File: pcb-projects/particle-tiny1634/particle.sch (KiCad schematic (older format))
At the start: 31 parts, among them CON1 AVR-ISP-6, IC1 ATTINY1634-SU, P1 TXN, P2 RXN, P3 TXS, P4 RXS, P5 TRX-CH, P6 TEST1-3

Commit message: added all 3d models, pcb cosmetics
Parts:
- FB1, FB2: footprint SMD_Packages:SMD-2010_Pol -> SMD_Packages:SMD-1206_Pol
- P1, P2: footprint SMT_PIN_HEADER:CONN-8_1-4 -> SMT_PIN_HEADER:CONN-6_1-3; symbol CONN_01X04 -> CONN_01X03
- P3, P4: footprint SMT_PIN_HEADER:CONN-8_5-8 -> SMT_PIN_HEADER:CONN-6_4-6; symbol CONN_02X04 -> CONN_02X03
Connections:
- net GND: now also P4.6 (P6); no longer P1.2 (P2), P4.7 (P7), P4.8 (P8)
- net RX-SOUTH: now also P4.4 (P4); no longer P4.5 (P5)
- net TX-NORTH: now also P1.3 (P3); no longer P1.4 (P4)
- net TX-SOUTH: now also P3.6 (P6); no longer P3.8 (P8)
- net VCC: now also P3.4 (P4); no longer P2.4 (P4), P3.5 (P5), P3.6 (P6)
- no-connect marks 12 -> 10
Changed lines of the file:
@@
 L VCC #PWR013
 U 1 1 568B8C3F
-P 5800 5100
-F 0 "#PWR013" H 5800 4950 50  0001 C CNN
-F 1 "VCC" H 5800 5250 50  0000 C CNN
-F 2 "" H 5800 5100 50  0000 C CNN
-F 3 "" H 5800 5100 50  0000 C CNN
-	1    5800 5100
-	1    0    0    -1
-$EndComp
-Text Label 4650 4550 0    60   ~ 0
+P 5500 5450
+F 0 "#PWR013" H 5500 5300 50  0001 C CNN
+F 1 "VCC" H 5500 5600 50  0000 C CNN
+F 2 "" H 5500 5450 50  0000 C CNN
+F 3 "" H 5500 5450 50  0000 C CNN
+	1    5500 5450
+	1    0    0    -1
+$EndComp
+Text Label 5850 4600 2    60   ~ 0
 RX-SOUTH
 $Comp
-L CONN_01X04 P2
+L CONN_01X03 P2
 U 1 1 568B98FD
-P 5650 2100
-F 0 "P2" H 5650 2350 50  0000 C CNN
-F 1 "RXN" V 5750 2100 50  0000 C CNN
-F 2 "SMT_PIN_HEADER:CONN-8_1-4" H 5650 2100 50  0001 C CNN
-F 3 "" H 5650 2100 50  0000 C CNN
-	1    5650 2100
+P 5650 2050
+F 0 "P2" H 5650 2300 50  0000 C CNN
+F 1 "RXN" V 5750 2050 50  0000 C CNN
+F 2 "SMT_PIN_HEADER:CONN-6_1-3" H 5650 2050 50  0001 C CNN
+F 3 "" H 5650 2050 50  0000 C CNN
+	1    5650 2050
 	1    0    0    -1
 $EndComp
@@
 L VCC #PWR014
 U 1 1 568B9905
-P 5200 2250
-F 0 "#PWR014" H 5200 2100 50  0001 C CNN
-F 1 "VCC" H 5200 2400 50  0000 C CNN
-F 2 "" H 5200 2250 50  0000 C CNN
-F 3 "" H 5200 2250 50  0000 C CNN
-	1    5200 2250
+P 5200 2150
+F 0 "#PWR014" H 5200 2000 50  0001 C CNN
+F 1 "VCC" H 5200 2300 50  0000 C CNN
+F 2 "" H 5200 2150 50  0000 C CNN
+F 3 "" H 5200 2150 50  0000 C CNN
+	1    5200 2150
 	1    0    0    -1
 $EndComp
 NoConn ~ 5450 2050
 $Comp
-L CONN_01X04 P1
+L CONN_01X03 P1
 U 1 1 568B990C
-P 5650 2700
-F 0 "P1" H 5650 2950 50  0000 C CNN
-F 1 "TXN" V 5750 2700 50  0000 C CNN
-F 2 "SMT_PIN_HEADER:CONN-8_1-4" H 5650 2700 50  0001 C CNN
-F 3 "" H 5650 2700 50  0000 C CNN
-	1    5650 2700
+P 5650 2750
+F 0 "P1" H 5650 3000 50  0000 C CNN
+F 1 "TXN" V 5750 2750 50  0000 C CNN
+F 2 "SMT_PIN_HEADER:CONN-6_1-3" H 5650 2750 50  0001 C CNN
+F 3 "" H 5650 2750 50  0000 C CNN
+	1    5650 2750
 	1    0    0    -1
 $EndComp
@@
 L GND #PWR016
 U 1 1 568BA31C
-P 5200 4800
-F 0 "#PWR016" H 5200 4550 50  0001 C CNN
-F 1 "GND" H 5200 4650 50  0000 C CNN
-F 2 "" H 5200 4800 50  0000 C CNN
-F 3 "" H 5200 4800 50  0000 C CNN
-	1    5200 4800
-	1    0    0    -1
-$EndComp
-Text Label 4650 5700 0    60   ~ 0
+P 5500 4700
+F 0 "#PWR016" H 5500 4450 50  0001 C CNN
+F 1 "GND" H 5500 4550 50  0000 C CNN
+F 2 "" H 5500 4700 50  0000 C CNN
+F 3 "" H 5500 4700 50  0000 C CNN
+	1    5500 4700
+	1    0    0    -1
+$EndComp
+Text Label 5850 5550 2    60   ~ 0
 TX-SOUTH
-NoConn ~ 5200 4350
-NoConn ~ 5200 4450
-NoConn ~ 5700 4350
-NoConn ~ 5700 4450
-$Comp
-L CONN_02X04 P3
+NoConn ~ 4800 4500
+NoConn ~ 5300 4500
+$Comp
+L CONN_02X03 P3
 U 1 1 568BB764
-P 5500 5400
-F 0 "P3" H 5500 5650 50  0000 C CNN
-F 1 "TXS" H 5500 5150 50  0000 C CNN
-F 2 "SMT_PIN_HEADER:CONN-8_5-8" H 5500 4200 50  0001 C CNN
-F 3 "" H 5500 4200 50  0000 C CNN
-	1    5500 5400
-	1    0    0    -1
-$EndComp
-NoConn ~ 5250 5250
-NoConn ~ 5250 5350
-NoConn ~ 5750 5250
-NoConn ~ 5750 5350
+P 5050 5450
+F 0 "P3" H 5050 5700 50  0000 C CNN
+F 1 "TXS" H 5050 5200 50  0000 C CNN
+F 2 "SMT_PIN_HEADER:CONN-6_4-6" H 5050 4250 50  0001 C CNN
+F 3 "" H 5050 4250 50  0000 C CNN
+	1    5050 5450
+	1    0    0    -1
+$EndComp
+NoConn ~ 4800 5350
+NoConn ~ 5300 5350
 NoConn ~ 5450 2750
-NoConn ~ 5700 4550
-$Comp
-L CONN_02X04 P4
+$Comp
+L CONN_02X03 P4
 U 1 1 568BB28B
-P 5450 4500
-F 0 "P4" H 5450 4750 50  0000 C CNN
-F 1 "RXS" H 5450 4250 50  0000 C CNN
-F 2 "SMT_PIN_HEADER:CONN-8_5-8" H 5450 3300 50  0001 C CNN
-F 3 "" H 5450 3300 50  0000 C CNN
-	1    5450 4500
-	1    0    0    -1
-$EndComp
-NoConn ~ 5250 5550
+P 5050 4600
+F 0 "P4" H 5050 4850 50  0000 C CNN
+F 1 "RXS" H 5050 4350 50  0000 C CNN
+F 2 "SMT_PIN_HEADER:CONN-6_4-6" H 5050 3400 50  0001 C CNN
+F 3 "" H 5050 3400 50  0000 C CNN
+	1    5050 4600
+	1    0    0    -1
+$EndComp
+NoConn ~ 4800 5550
 $Comp
 L GND #PWR017
@@
 F 0 "FB1" H 7000 2550 50  0000 C CNN
 F 1 "TXN-SMA" H 7000 2300 50  0000 C CNN
-F 2 "SMD_Packages:SMD-2010_Pol" H 7000 2400 50  0001 C CNN
+F 2 "SMD_Packages:SMD-1206_Pol" H 7000 2400 50  0001 C CNN
 F 3 "" H 7000 2400 50  0000 C CNN
 	1    7000 2400
@@
 F 0 "FB2" H 7000 5350 50  0000 C CNN
 F 1 "TXS-SMA" H 7000 5100 50  0000 C CNN
-F 2 "SMD_Packages:SMD-2010_Pol" H 7000 5200 50  0001 C CNN
+F 2 "SMD_Packages:SMD-1206_Pol" H 7000 5200 50  0001 C CNN
 F 3 "" H 7000 5200 50  0000 C CNN
 	1    7000 5200
@@
 	7350 5850 7500 5850
 Wire Wire Line
-	4650 5700 5800 5700
+	5300 5550 5850 5550
 Wire Wire Line
 	4650 1950 5450 1950
 Wire Wire Line
-	5200 2250 5450 2250
+	5200 2150 5450 2150
 Wire Wire Line
 	5450 2550 5200 2550
 Wire Wire Line
-	5450 2250 5450 2150
-Wire Wire Line
 	9400 3450 8900 3450
 Wire Wire Line
 	8900 3550 9400 3550
 Wire Wire Line
-	4650 4550 5200 4550
+	5850 4600 5300 4600
 Wire Wire Line
 	4650 2850 5450 2850
@@
 	5450 2650 5450 2550
 Wire Wire Line
-	5700 4800 5700 4650
-Wire Wire Line
-	5200 4800 5700 4800
-Wire Wire Line
-	5200 4650 5200 4800
-Wire Wire Line
-	5800 5450 5750 5450
-Wire Wire Line
-	5800 5100 5800 5450
-Wire Wire Line
-	5800 5100 5200 5100
-Wire Wire Line
-	5200 5100 5200 5450
-Wire Wire Line
-	5200 5450 5250 5450
+	5300 4700 5500 4700
+Wire Wire Line
+	5300 5450 5500 5450
 Connection ~ 7400 5850
 Connection ~ 7400 3000
@@
 	3750 3600 2800 3600
 Wire Wire Line
-	5750 5550 5800 5550
-Wire Wire Line
-	5800 5550 5800 5700
+	5400 5550 5400 5550
 $Comp
 L R R14
@@
 Text Label 4100 7450 0    60   ~ 0
 TP3
+NoConn ~ 4800 4600
+NoConn ~ 4800 4700
+NoConn ~ 4800 5450
 $EndSCHEMATC

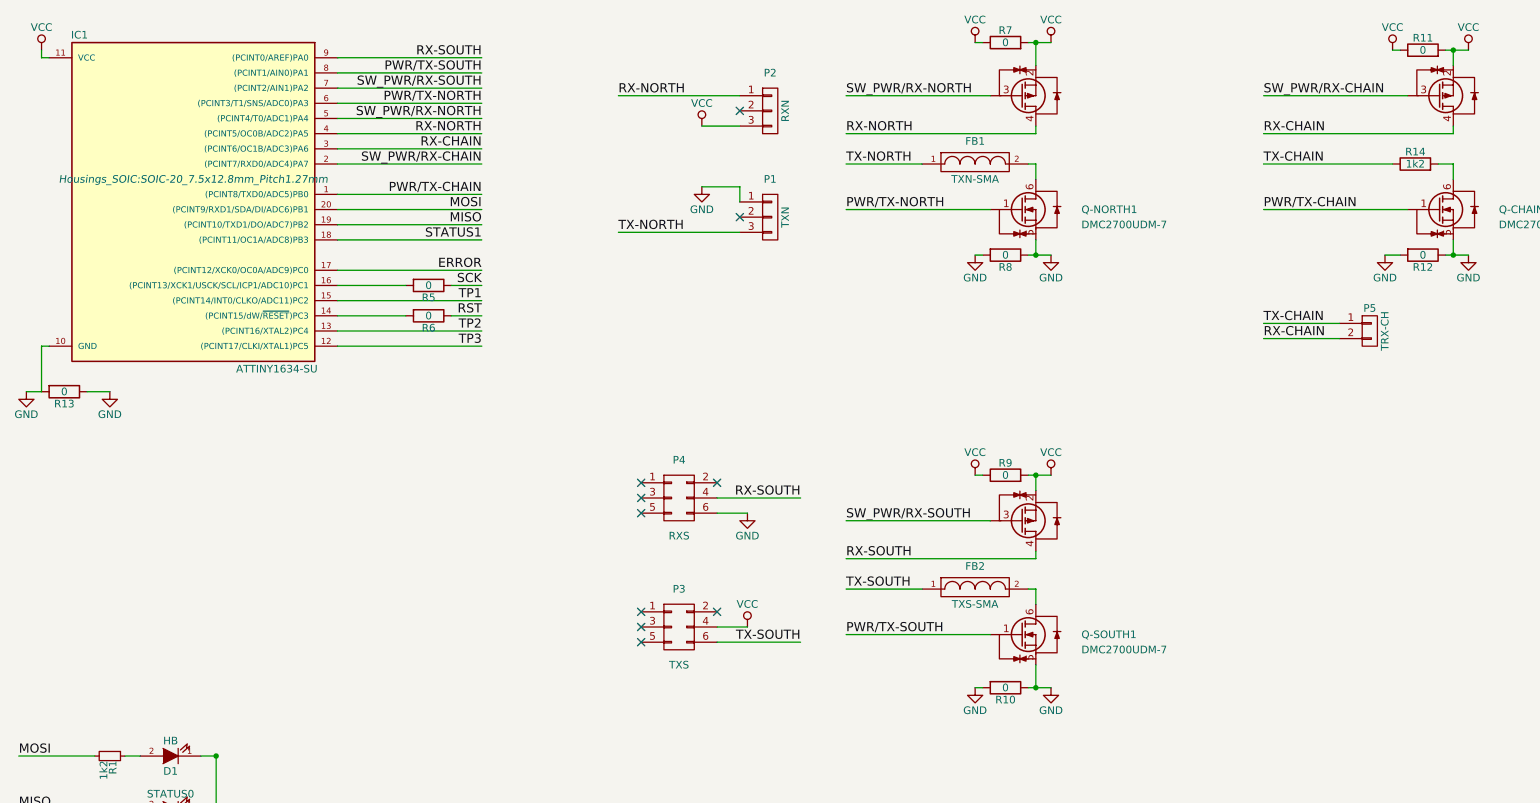
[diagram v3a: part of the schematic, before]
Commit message: added bill of material
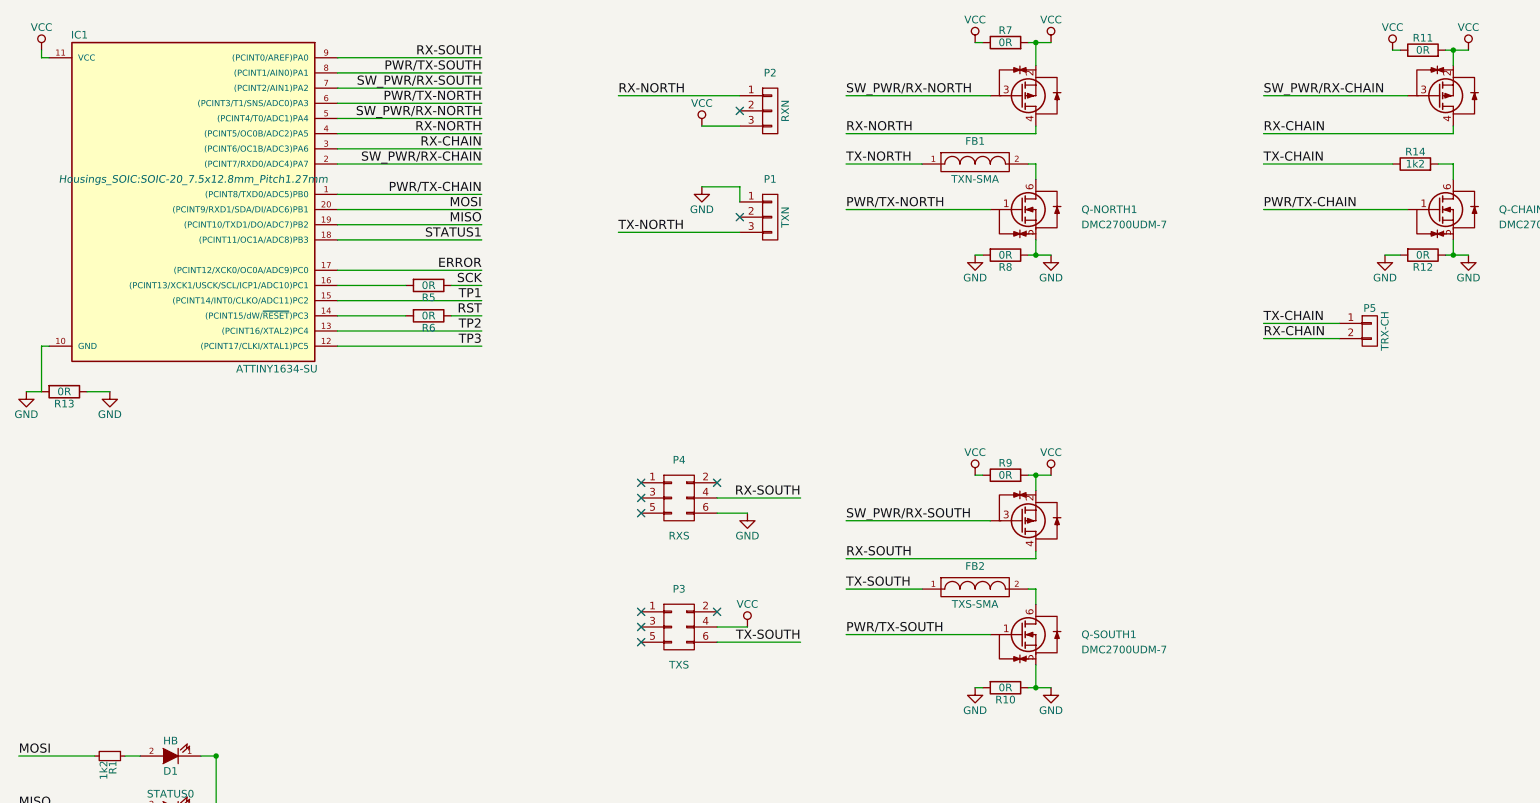
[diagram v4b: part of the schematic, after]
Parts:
- CON1: price (none) -> 2row-20pole-10pcs/pkg 10-40pcs 2.177; supplyer (none) -> http://at.rs-online.com/web/p/leiterplatten-header/5286417/
- D1: price (none) -> 25-100pcs 0.154; supplyer (none) -> http://at.rs-online.com/web/p/leds-sichtbares-licht/7269225/
- D2: price (none) -> 25-100pcs 0.14; supplyer (none) -> http://at.rs-online.com/web/p/leds-sichtbares-licht/7269215/
- D4: price (none) -> 25-100pcs 0.197; supplyer (none) -> http://at.rs-online.com/web/p/leds-sichtbares-licht/7269212/
- FB1: price (none) -> <240pcs 0.733; supplyer (none) -> http://at.rs-online.com/web/p/anzeigen-gluehlampen/0106458/
- IC1: price (none) -> rs attiny1634R-su 2-8pcs 1.84 >10pcs 1.725 farnell attiny16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; supplyer (none) -> http://at.rs-online.com/web/p/mikrocontroller/7617703/
- P6: price (none) -> 1row-5pcs-40pol/pkg 1.324; supplyer (none) -> http://at.rs-online.com/web/p/leiterplatten-header/0155901/
- Q-NORTH1: price (none) -> 20-80pcs 0.1291 >100pcs 0.132; supplyer (none) -> http://at.rs-online.com/web/p/transistoren-mosfet/8232918/
- R10, R11, R12, R13, R5, R6, R8, R9: value 0 -> 0R
- R14: price (none) -> < 5pkg @ 100pcs 1.72 per pkg; supplyer (none) -> http://at.rs-online.com/web/p/smd-widerstande/8071158/
- R7: value 0 -> 0R; price (none) -> <450pcs 0.016; supplyer (none) -> http://at.rs-online.com/web/p/smd-widerstande/7409104/
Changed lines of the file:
@@
 F 2 "Housings_SOIC:SOIC-20_7.5x12.8mm_Pitch1.27mm" H 1850 3000 50  0000 C CIN
 F 3 "" H 1850 3200 50  0000 C CNN
+F 4 "http://at.rs-online.com/web/p/mikrocontroller/7617703/" H 1850 2750 60  0001 C CNN "supplyer"
+F 5 "rs attiny1634R-su 2-8pcs 1.84 >10pcs 1.725 farnell attiny1634-su <10pcs 1.44 <25pcs 1.35" H 1850 2750 60  0001 C CNN "price"
 	1    1850 2750
 	1    0    0    -1
@@
 F 2 "Resistors_SMD:R_1206_HandSoldering" H 1700 6300 50  0001 C CNN
 F 3 "" H 1700 6300 50  0000 C CNN
+F 4 "http://at.rs-online.com/web/p/leds-sichtbares-licht/7269225/" H 1700 6300 60  0001 C CNN "supplyer"
+F 5 "25-100pcs 0.154" H 1700 6300 60  0001 C CNN "price"
 	1    1700 6300
 	-1   0    0    1
@@
 F 2 "Resistors_SMD:R_1206_HandSoldering" H 1700 6650 50  0001 C CNN
 F 3 "" H 1700 6650 50  0000 C CNN
+F 4 "http://at.rs-online.com/web/p/leds-sichtbares-licht/7269215/" H 1700 6650 60  0001 C CNN "supplyer"
+F 5 "25-100pcs 0.14" H 1700 6650 60  0001 C CNN "price"
 	1    1700 6650
 	-1   0    0    1
@@
 F 2 "Resistors_SMD:R_1206_HandSoldering" H 1700 7350 50  0001 C CNN
 F 3 "" H 1700 7350 50  0000 C CNN
+F 4 "http://at.rs-online.com/web/p/leds-sichtbares-licht/7269212/" H 1700 7350 60  0001 C CNN "supplyer"
+F 5 "25-100pcs 0.197 " H 1700 7350 60  0001 C CNN "price"
 	1    1700 7350
 	-1   0    0    1
@@
 F 2 "SMT_PIN_HEADER:CONN-6" V 2530 7390 50  0001 C CNN
 F 3 "" H 3025 7350 50  0000 C CNN
+F 4 "http://at.rs-online.com/web/p/leiterplatten-header/5286417/" H 3050 7350 60  0001 C CNN "supplyer"
+F 5 "2row-20pole-10pcs/pkg 10-40pcs 2.177" H 3050 7350 60  0001 C CNN "price"
 	1    3050 7350
 	-1   0    0    1
@@
 P 7200 3000
 F 0 "R8" V 7280 3000 50  0000 C CNN
-F 1 "0" V 7200 3000 50  0000 C CNN
+F 1 "0R" V 7200 3000 50  0000 C CNN
 F 2 "Resistors_SMD:R_1206_HandSoldering" V 7130 3000 50  0001 C CNN
 F 3 "" H 7200 3000 50  0000 C CNN
@@
 P 7200 1600
 F 0 "R7" V 7280 1600 50  0000 C CNN
-F 1 "0" V 7200 1600 50  0000 C CNN
+F 1 "0R" V 7200 1600 50  0000 C CNN
 F 2 "Resistors_SMD:R_1206_HandSoldering" V 7130 1600 50  0001 C CNN
 F 3 "" H 7200 1600 50  0000 C CNN
+F 4 "http://at.rs-online.com/web/p/smd-widerstande/7409104/" V 7200 1600 60  0001 C CNN "supplyer"
+F 5 "<450pcs 0.016" V 7200 1600 60  0001 C CNN "price"
 	1    7200 1600
 	0    -1   -1   0
@@
 P 7200 4450
 F 0 "R9" V 7280 4450 50  0000 C CNN
-F 1 "0" V 7200 4450 50  0000 C CNN
+F 1 "0R" V 7200 4450 50  0000 C CNN
 F 2 "Resistors_SMD:R_1206_HandSoldering" V 7130 4450 50  0001 C CNN
 F 3 "" H 7200 4450 50  0000 C CNN
@@
 P 9950 1650
 F 0 "R11" V 10030 1650 50  0000 C CNN
-F 1 "0" V 9950 1650 50  0000 C CNN
+F 1 "0R" V 9950 1650 50  0000 C CNN
 F 2 "Resistors_SMD:R_1206_HandSoldering" V 9880 1650 50  0001 C CNN
 F 3 "" H 9950 1650 50  0000 C CNN
@@
 P 9950 3000
 F 0 "R12" V 10030 3000 50  0000 C CNN
-F 1 "0" V 9950 3000 50  0000 C CNN
+F 1 "0R" V 9950 3000 50  0000 C CNN
 F 2 "Resistors_SMD:R_1206_HandSoldering" V 9880 3000 50  0001 C CNN
 F 3 "" H 9950 3000 50  0000 C CNN
@@
 P 7200 5850
 F 0 "R10" V 7280 5850 50  0000 C CNN
-F 1 "0" V 7200 5850 50  0000 C CNN
+F 1 "0R" V 7200 5850 50  0000 C CNN
 F 2 "Resistors_SMD:R_1206_HandSoldering" V 7130 5850 50  0001 C CNN
 F 3 "" H 7200 5850 50  0000 C CNN
@@
 P 3400 3400
 F 0 "R6" V 3480 3400 50  0000 C CNN
-F 1 "0" V 3400 3400 50  0000 C CNN
+F 1 "0R" V 3400 3400 50  0000 C CNN
 F 2 "Resistors_SMD:R_1206_HandSoldering" V 3330 3400 50  0001 C CNN
 F 3 "" H 3400 3400 50  0000 C CNN
@@
 P 3400 3200
 F 0 "R5" V 3480 3200 50  0000 C CNN
-F 1 "0" V 3400 3200 50  0000 C CNN
+F 1 "0R" V 3400 3200 50  0000 C CNN
 F 2 "Resistors_SMD:R_1206_HandSoldering" V 3330 3200 50  0001 C CNN
 F 3 "" H 3400 3200 50  0000 C CNN
@@
 P 1000 3900
 F 0 "R13" V 1080 3900 50  0000 C CNN
-F 1 "0" V 1000 3900 50  0000 C CNN
+F 1 "0R" V 1000 3900 50  0000 C CNN
 F 2 "Resistors_SMD:R_1206_HandSoldering" V 930 3900 50  0001 C CNN
 F 3 "" H 1000 3900 50  0000 C CNN
@@
 F 2 "SMD_Packages:SMD-1206_Pol" H 7000 2400 50  0001 C CNN
 F 3 "" H 7000 2400 50  0000 C CNN
+F 4 "http://at.rs-online.com/web/p/anzeigen-gluehlampen/0106458/" H 7000 2400 60  0001 C CNN "supplyer"
+F 5 "<240pcs 0.733" H 7000 2400 60  0001 C CNN "price"
 	1    7000 2400
 	1    0    0    -1
@@
 F 2 "sot26:SOT-26" H 7470 2580 50  0001 C CNN
 F 3 "" H 7300 2700 50  0000 C CNN
+F 4 "http://at.rs-online.com/web/p/transistoren-mosfet/8232918/" H 7300 2700 60  0001 C CNN "supplyer"
+F 5 "20-80pcs 0.1291 >100pcs 0.132" H 7300 2700 60  0001 C CNN "price"
 	1    7300 2700
 	1    0    0    -1
@@
 F 2 "Resistors_SMD:R_1206_HandSoldering" V 9830 2400 50  0001 C CNN
 F 3 "" H 9900 2400 50  0000 C CNN
+F 4 "http://at.rs-online.com/web/p/smd-widerstande/8071158/" V 9900 2400 60  0001 C CNN "supplyer"
+F 5 "< 5pkg @ 100pcs 1.72 per pkg" V 9900 2400 60  0001 C CNN "price"
 	1    9900 2400
 	0    -1   -1   0
@@
 F 2 "SMT_PIN_HEADER:CONN-1x3" H 4500 7350 50  0001 C CNN
 F 3 "" H 4500 7350 50  0000 C CNN
+F 4 "http://at.rs-online.com/web/p/leiterplatten-header/0155901/" H 4500 7350 60  0001 C CNN "supplyer"
+F 5 "1row-5pcs-40pol/pkg 1.324" H 4500 7350 60  0001 C CNN "price"
 	1    4500 7350
 	1    0    0    -1
